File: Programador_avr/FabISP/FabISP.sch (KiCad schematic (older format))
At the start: 7 parts

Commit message: componentes completos
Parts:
- removed IC?: REGULATORSOT23, fab:fab-SOT23, symbol fab:REGULATORSOT23
- added D? (x3): DIODESOD123, fab:fab-SOD123, symbol fab:DIODESOD123
- added R?: RES-US1206FAB, fab:fab-R1206FAB, symbol fab:RES-US1206FAB
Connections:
- net labels added: GND, VCC
- wire segments 0 -> 3
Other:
- moved on the sheet: C?, JP?, M?, U?
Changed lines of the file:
@@
 L fab:ATSAMD11D14A-SS U?
 U 1 1 5F6E3135
-P 2350 1950
-F 0 "U?" H 2350 2931 50  0000 C CNN
-F 1 "ATSAMD11D14A-SS" H 2350 2840 50  0000 C CNN
-F 2 "fab:fab-SOIC-20_7.5x12.8mm_P1.27mm" H 2350 800 50  0001 C CNN
-F 3 "" H 2350 1050 50  0001 C CNN
-	1    2350 1950
+P 3100 1650
+F 0 "U?" H 3450 2400 50  0000 C CNN
+F 1 "ATSAMD11D14A-SS" H 3050 2400 50  0000 C CNN
+F 2 "fab:fab-SOIC-20_7.5x12.8mm_P1.27mm" H 3100 500 50  0001 C CNN
+F 3 "" H 3100 750 50  0001 C CNN
+	1    3100 1650
 	1    0    0    -1
 $EndComp
@@
 L fab:USB_MINIB M?
 U 1 1 5F6E4482
-P 1250 1900
-F 0 "M?" H 1250 1900 45  0001 C CNN
-F 1 "USB_MINIB" H 1250 1900 45  0001 C CNN
-F 2 "fab:fab-USB_MINIB" H 1280 2050 20  0001 C CNN
-F 3 "" H 1250 1900 50  0001 C CNN
-	1    1250 1900
-	-1   0    0    1
+P 1150 1900
+F 0 "M?" H 1379 1792 45  0001 L CNN
+F 1 "USB_MINIB" H 1150 1900 45  0001 C CNN
+F 2 "fab:fab-USB_MINIB" H 1180 2050 20  0001 C CNN
+F 3 "" H 1150 1900 50  0001 C CNN
+	1    1150 1900
+	0    -1   -1   0
 $EndComp
 $Comp
@@
 L fab:RESONATOR M?
 U 1 1 5F6E8255
-P 4700 1700
-F 0 "M?" H 4700 1954 45  0000 C CNN
-F 1 "RESONATOR" H 4700 1870 45  0000 C CNN
-F 2 "fab:fab-EFOBM" H 4730 1850 20  0001 C CNN
-F 3 "" H 4700 1700 50  0001 C CNN
-	1    4700 1700
+P 5300 1100
+F 0 "M?" H 5300 1354 45  0000 C CNN
+F 1 "RESONATOR" H 5300 1270 45  0000 C CNN
+F 2 "fab:fab-EFOBM" H 5330 1250 20  0001 C CNN
+F 3 "" H 5300 1100 50  0001 C CNN
+	1    5300 1100
 	1    0    0    -1
 $EndComp
@@
 L fab:PINHD-2X3-SMD JP?
 U 1 1 5F6E99D1
-P 4650 2600
-F 0 "JP?" H 4700 2954 45  0000 C CNN
-F 1 "PINHD-2X3-SMD" H 4700 2870 45  0000 C CNN
-F 2 "fab:fab-2X03SMD" H 4680 2750 20  0001 C CNN
-F 3 "" H 4650 2600 50  0001 C CNN
-	1    4650 2600
-	1    0    0    -1
-$EndComp
-$Comp
-L fab:REGULATORSOT23 IC?
-U 1 1 5F6EA6B2
-P 5750 2000
-F 0 "IC?" H 5750 2354 45  0000 C CNN
-F 1 "REGULATORSOT23" H 5750 2270 45  0000 C CNN
-F 2 "fab:fab-SOT23" H 5780 2150 20  0001 C CNN
-F 3 "" H 5750 2000 50  0001 C CNN
-	1    5750 2000
+P 2100 2400
+F 0 "JP?" H 2150 2754 45  0000 C CNN
+F 1 "PINHD-2X3-SMD" H 2150 2670 45  0000 C CNN
+F 2 "fab:fab-2X03SMD" H 2130 2550 20  0001 C CNN
+F 3 "" H 2100 2400 50  0001 C CNN
+	1    2100 2400
 	1    0    0    -1
 $EndComp
@@
 L fab:CAP-US1206FAB C?
 U 1 1 5F6EB467
-P 3600 2800
-F 0 "C?" H 3650 3054 45  0000 C CNN
-F 1 "CAP-US1206FAB" H 3650 2970 45  0000 C CNN
-F 2 "fab:fab-C1206FAB" H 3630 2950 20  0001 C CNN
-F 3 "" H 3600 2800 50  0001 C CNN
-	1    3600 2800
+P 1750 1300
+F 0 "C?" V 1758 1428 45  0000 L CNN
+F 1 "CAP-US1206FAB" V 1842 1428 45  0000 L CNN
+F 2 "fab:fab-C1206FAB" H 1780 1450 20  0001 C CNN
+F 3 "" H 1750 1300 50  0001 C CNN
+	1    1750 1300
+	0    1    1    0
+$EndComp
+$Comp
+L fab:DIODESOD123 D?
+U 1 1 5F6EC2CB
+P 5150 2200
+F 0 "D?" V 5192 2122 45  0000 R CNN
+F 1 "DIODESOD123" V 5108 2122 45  0000 R CNN
+F 2 "fab:fab-SOD123" H 5180 2350 20  0001 C CNN
+F 3 "" H 5150 2200 50  0001 C CNN
+	1    5150 2200
+	0    -1   -1   0
+$EndComp
+$Comp
+L power:VCC #PWR?
+U 1 1 5F6EDF62
+P 1500 1100
+F 0 "#PWR?" H 1500 950 50  0001 C CNN
+F 1 "VCC" H 1517 1273 50  0000 C CNN
+F 2 "" H 1500 1100 50  0001 C CNN
+F 3 "" H 1500 1100 50  0001 C CNN
+	1    1500 1100
 	1    0    0    -1
 $EndComp
+$Comp
+L power:GND #PWR?
+U 1 1 5F6EEE4A
+P 3100 2450
+F 0 "#PWR?" H 3100 2200 50  0001 C CNN
+F 1 "GND" H 3105 2277 50  0000 C CNN
+F 2 "" H 3100 2450 50  0001 C CNN
+F 3 "" H 3100 2450 50  0001 C CNN
+	1    3100 2450
+	1    0    0    -1
+$EndComp
+$Comp
+L power:VCC #PWR?
+U 1 1 5F6F2122
+P 3100 850
+F 0 "#PWR?" H 3100 700 50  0001 C CNN
+F 1 "VCC" H 3117 1023 50  0000 C CNN
+F 2 "" H 3100 850 50  0001 C CNN
+F 3 "" H 3100 850 50  0001 C CNN
+	1    3100 850
+	1    0    0    -1
+$EndComp
+$Comp
+L fab:RES-US1206FAB R?
+U 1 1 5F6FE07F
+P 1350 2250
+F 0 "R?" V 1308 2318 45  0000 L CNN
+F 1 "RES-US1206FAB" H 950 2200 45  0000 L CNN
+F 2 "fab:fab-R1206FAB" H 1380 2400 20  0001 C CNN
+F 3 "" H 1350 2250 50  0001 C CNN
+	1    1350 2250
+	-1   0    0    1
+$EndComp
+$Comp
+L fab:DIODESOD123 D?
+U 1 1 5F700804
+P 1150 2450
+F 0 "D?" V 1108 2528 45  0000 L CNN
+F 1 "DIODESOD123" V 1192 2528 45  0000 L CNN
+F 2 "fab:fab-SOD123" H 1180 2600 20  0001 C CNN
+F 3 "" H 1150 2450 50  0001 C CNN
+	1    1150 2450
+	0    1    1    0
+$EndComp
+Wire Wire Line
+	1150 2000 1150 2250
+Wire Wire Line
+	1150 2350 1150 2250
+Connection ~ 1150 2250
+$Comp
+L power:GND #PWR?
+U 1 1 5F7029DD
+P 1150 2700
+F 0 "#PWR?" H 1150 2450 50  0001 C CNN
+F 1 "GND" H 1155 2527 50  0000 C CNN
+F 2 "" H 1150 2700 50  0001 C CNN
+F 3 "" H 1150 2700 50  0001 C CNN
+	1    1150 2700
+	1    0    0    -1
+$EndComp
+Wire Wire Line
+	1150 2550 1150 2700
+$Comp
+L fab:DIODESOD123 D?
+U 1 1 5F70324B
+P 950 2450
+F 0 "D?" V 908 2528 45  0000 L CNN
+F 1 "DIODESOD123" V 992 2528 45  0000 L CNN
+F 2 "fab:fab-SOD123" H 980 2600 20  0001 C CNN
+F 3 "" H 950 2450 50  0001 C CNN
+	1    950  2450
+	0    1    1    0
+$EndComp
 $EndSCHEMATC

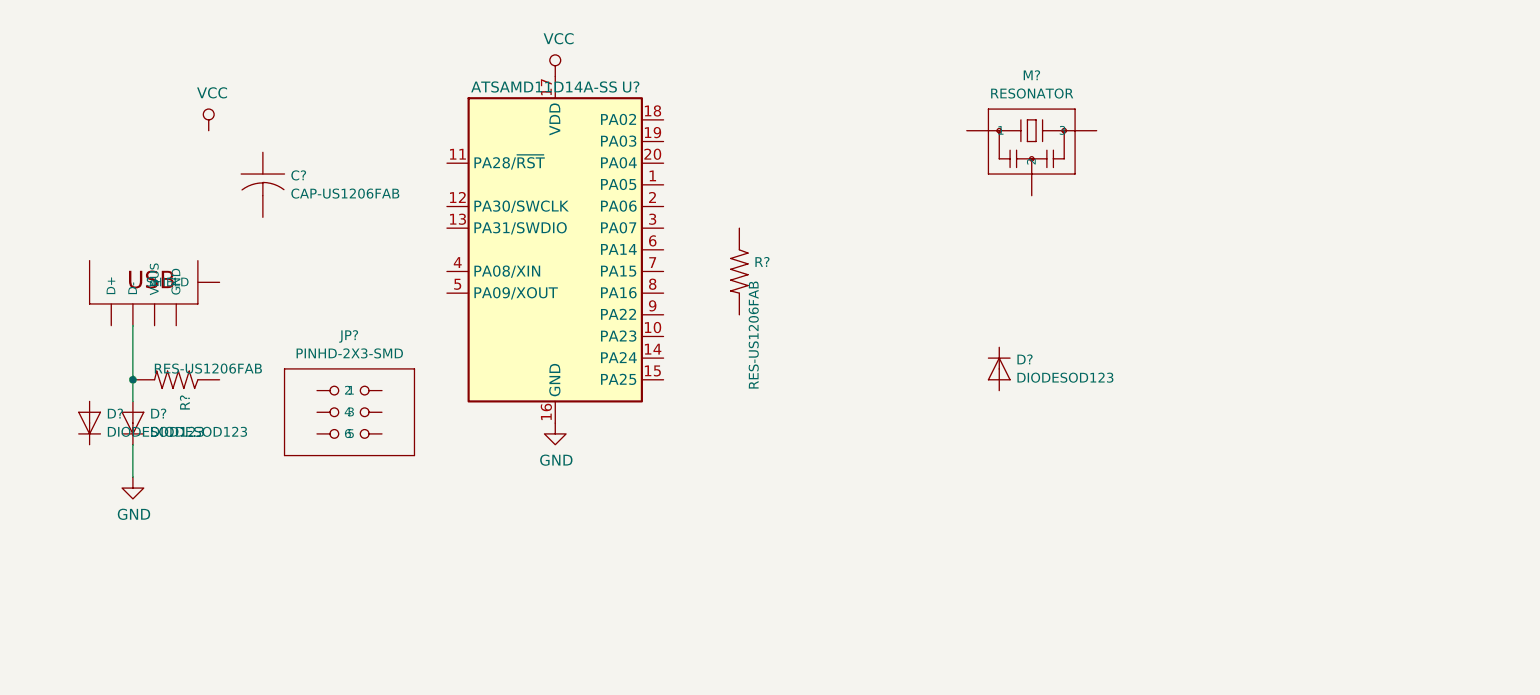
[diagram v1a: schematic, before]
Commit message: Conexiones USB
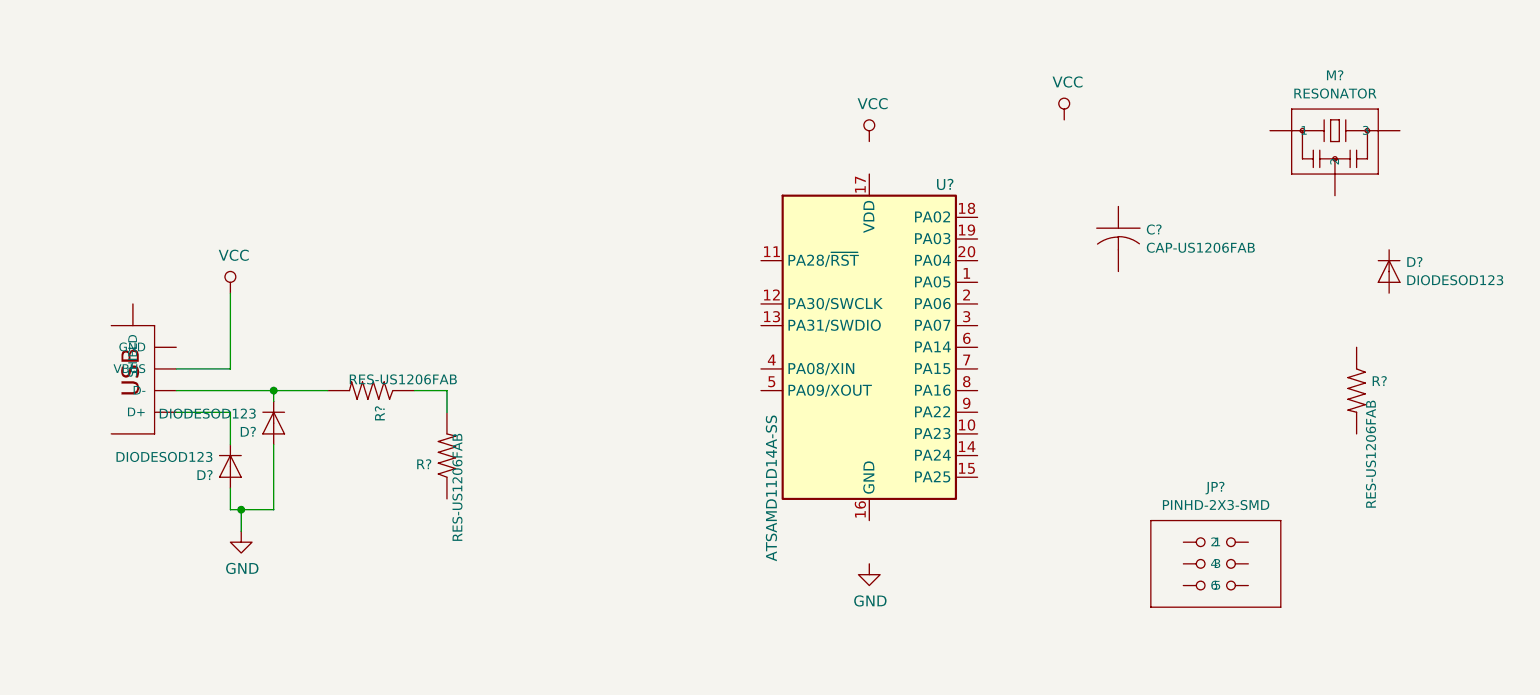
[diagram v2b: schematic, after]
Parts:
- added R?: RES-US1206FAB, fab:fab-R1206FAB, symbol fab:RES-US1206FAB
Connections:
- net GND: now also D?.ANODE (A), D?.ANODE (A); no longer D?.CATHODE (C), U?.16 (GND)
- net VCC: now also M?.VBUS; no longer U?.17 (VDD)
- net at M?.D+: now also D?.CATHODE (C)
- net at M?.D-, R?.2: now also D?.CATHODE (C); no longer D?.ANODE (A)
- net at R?.1: now also R?.2
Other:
- moved on the sheet: C?, D?, JP?, M?, R?, U?
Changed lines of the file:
@@
 EESchema Schematic File Version 4
+LIBS:FabISP-cache
 EELAYER 30 0
 EELAYER END
@@
 L fab:ATSAMD11D14A-SS U?
 U 1 1 5F6E3135
-P 3100 1650
-F 0 "U?" H 3450 2400 50  0000 C CNN
-F 1 "ATSAMD11D14A-SS" H 3050 2400 50  0000 C CNN
-F 2 "fab:fab-SOIC-20_7.5x12.8mm_P1.27mm" H 3100 500 50  0001 C CNN
-F 3 "" H 3100 750 50  0001 C CNN
-	1    3100 1650
+P 4550 2100
+F 0 "U?" H 4900 2850 50  0000 C CNN
+F 1 "ATSAMD11D14A-SS" V 4100 1450 50  0000 C CNN
+F 2 "fab:fab-SOIC-20_7.5x12.8mm_P1.27mm" H 4550 950 50  0001 C CNN
+F 3 "" H 4550 1200 50  0001 C CNN
+	1    4550 2100
 	1    0    0    -1
 $EndComp
@@
 L fab:USB_MINIB M?
 U 1 1 5F6E4482
-P 1150 1900
-F 0 "M?" H 1379 1792 45  0001 L CNN
-F 1 "USB_MINIB" H 1150 1900 45  0001 C CNN
-F 2 "fab:fab-USB_MINIB" H 1180 2050 20  0001 C CNN
-F 3 "" H 1150 1900 50  0001 C CNN
-	1    1150 1900
-	0    -1   -1   0
+P 1250 2300
+F 0 "M?" H 1479 2192 45  0001 L CNN
+F 1 "USB_MINIB" H 1250 2300 45  0001 C CNN
+F 2 "fab:fab-USB_MINIB" H 1280 2450 20  0001 C CNN
+F 3 "" H 1250 2300 50  0001 C CNN
+	1    1250 2300
+	-1   0    0    1
 $EndComp
 $Comp
 L fab:RES-US1206FAB R?
 U 1 1 5F6E5992
-P 3950 1750
-F 0 "R?" V 3908 1818 45  0000 L CNN
-F 1 "RES-US1206FAB" H 3992 1818 45  0000 L CNN
-F 2 "fab:fab-R1206FAB" H 3980 1900 20  0001 C CNN
-F 3 "" H 3950 1750 50  0001 C CNN
-	1    3950 1750
+P 6800 2300
+F 0 "R?" V 6758 2368 45  0000 L CNN
+F 1 "RES-US1206FAB" H 6842 2368 45  0000 L CNN
+F 2 "fab:fab-R1206FAB" H 6830 2450 20  0001 C CNN
+F 3 "" H 6800 2300 50  0001 C CNN
+	1    6800 2300
 	0    1    1    0
 $EndComp
@@
 L fab:RESONATOR M?
 U 1 1 5F6E8255
-P 5300 1100
-F 0 "M?" H 5300 1354 45  0000 C CNN
-F 1 "RESONATOR" H 5300 1270 45  0000 C CNN
-F 2 "fab:fab-EFOBM" H 5330 1250 20  0001 C CNN
-F 3 "" H 5300 1100 50  0001 C CNN
-	1    5300 1100
+P 6700 1100
+F 0 "M?" H 6700 1354 45  0000 C CNN
+F 1 "RESONATOR" H 6700 1270 45  0000 C CNN
+F 2 "fab:fab-EFOBM" H 6730 1250 20  0001 C CNN
+F 3 "" H 6700 1100 50  0001 C CNN
+	1    6700 1100
 	1    0    0    -1
 $EndComp
@@
 L fab:PINHD-2X3-SMD JP?
 U 1 1 5F6E99D1
-P 2100 2400
-F 0 "JP?" H 2150 2754 45  0000 C CNN
-F 1 "PINHD-2X3-SMD" H 2150 2670 45  0000 C CNN
-F 2 "fab:fab-2X03SMD" H 2130 2550 20  0001 C CNN
-F 3 "" H 2100 2400 50  0001 C CNN
-	1    2100 2400
+P 6100 3100
+F 0 "JP?" H 6150 3454 45  0000 C CNN
+F 1 "PINHD-2X3-SMD" H 6150 3370 45  0000 C CNN
+F 2 "fab:fab-2X03SMD" H 6130 3250 20  0001 C CNN
+F 3 "" H 6100 3100 50  0001 C CNN
+	1    6100 3100
 	1    0    0    -1
 $EndComp
@@
 L fab:CAP-US1206FAB C?
 U 1 1 5F6EB467
-P 1750 1300
-F 0 "C?" V 1758 1428 45  0000 L CNN
-F 1 "CAP-US1206FAB" V 1842 1428 45  0000 L CNN
-F 2 "fab:fab-C1206FAB" H 1780 1450 20  0001 C CNN
-F 3 "" H 1750 1300 50  0001 C CNN
-	1    1750 1300
+P 5700 1550
+F 0 "C?" V 5708 1678 45  0000 L CNN
+F 1 "CAP-US1206FAB" V 5792 1678 45  0000 L CNN
+F 2 "fab:fab-C1206FAB" H 5730 1700 20  0001 C CNN
+F 3 "" H 5700 1550 50  0001 C CNN
+	1    5700 1550
 	0    1    1    0
 $EndComp
@@
 L fab:DIODESOD123 D?
 U 1 1 5F6EC2CB
-P 5150 2200
-F 0 "D?" V 5192 2122 45  0000 R CNN
-F 1 "DIODESOD123" V 5108 2122 45  0000 R CNN
-F 2 "fab:fab-SOD123" H 5180 2350 20  0001 C CNN
-F 3 "" H 5150 2200 50  0001 C CNN
-	1    5150 2200
+P 6950 1750
+F 0 "D?" V 6992 1672 45  0000 R CNN
+F 1 "DIODESOD123" V 6908 1672 45  0000 R CNN
+F 2 "fab:fab-SOD123" H 6980 1900 20  0001 C CNN
+F 3 "" H 6950 1750 50  0001 C CNN
+	1    6950 1750
 	0    -1   -1   0
 $EndComp
@@
 L power:VCC #PWR?
 U 1 1 5F6EDF62
-P 1500 1100
-F 0 "#PWR?" H 1500 950 50  0001 C CNN
-F 1 "VCC" H 1517 1273 50  0000 C CNN
-F 2 "" H 1500 1100 50  0001 C CNN
-F 3 "" H 1500 1100 50  0001 C CNN
-	1    1500 1100
+P 5450 1050
+F 0 "#PWR?" H 5450 900 50  0001 C CNN
+F 1 "VCC" H 5467 1223 50  0000 C CNN
+F 2 "" H 5450 1050 50  0001 C CNN
+F 3 "" H 5450 1050 50  0001 C CNN
+	1    5450 1050
 	1    0    0    -1
 $EndComp
@@
 L power:GND #PWR?
 U 1 1 5F6EEE4A
-P 3100 2450
-F 0 "#PWR?" H 3100 2200 50  0001 C CNN
-F 1 "GND" H 3105 2277 50  0000 C CNN
-F 2 "" H 3100 2450 50  0001 C CNN
-F 3 "" H 3100 2450 50  0001 C CNN
-	1    3100 2450
+P 4550 3100
+F 0 "#PWR?" H 4550 2850 50  0001 C CNN
+F 1 "GND" H 4555 2927 50  0000 C CNN
+F 2 "" H 4550 3100 50  0001 C CNN
+F 3 "" H 4550 3100 50  0001 C CNN
+	1    4550 3100
 	1    0    0    -1
 $EndComp
@@
 L power:VCC #PWR?
 U 1 1 5F6F2122
-P 3100 850
-F 0 "#PWR?" H 3100 700 50  0001 C CNN
-F 1 "VCC" H 3117 1023 50  0000 C CNN
-F 2 "" H 3100 850 50  0001 C CNN
-F 3 "" H 3100 850 50  0001 C CNN
-	1    3100 850
+P 4550 1150
+F 0 "#PWR?" H 4550 1000 50  0001 C CNN
+F 1 "VCC" H 4567 1323 50  0000 C CNN
+F 2 "" H 4550 1150 50  0001 C CNN
+F 3 "" H 4550 1150 50  0001 C CNN
+	1    4550 1150
 	1    0    0    -1
 $EndComp
@@
 L fab:RES-US1206FAB R?
 U 1 1 5F6FE07F
-P 1350 2250
-F 0 "R?" V 1308 2318 45  0000 L CNN
-F 1 "RES-US1206FAB" H 950 2200 45  0000 L CNN
-F 2 "fab:fab-R1206FAB" H 1380 2400 20  0001 C CNN
-F 3 "" H 1350 2250 50  0001 C CNN
-	1    1350 2250
+P 2250 2300
+F 0 "R?" V 2208 2368 45  0000 L CNN
+F 1 "RES-US1206FAB" H 1850 2250 45  0000 L CNN
+F 2 "fab:fab-R1206FAB" H 2280 2450 20  0001 C CNN
+F 3 "" H 2250 2300 50  0001 C CNN
+	1    2250 2300
 	-1   0    0    1
 $EndComp
@@
 L fab:DIODESOD123 D?
 U 1 1 5F700804
-P 1150 2450
-F 0 "D?" V 1108 2528 45  0000 L CNN
-F 1 "DIODESOD123" V 1192 2528 45  0000 L CNN
-F 2 "fab:fab-SOD123" H 1180 2600 20  0001 C CNN
-F 3 "" H 1150 2450 50  0001 C CNN
-	1    1150 2450
-	0    1    1    0
-$EndComp
-Wire Wire Line
-	1150 2000 1150 2250
-Wire Wire Line
-	1150 2350 1150 2250
-Connection ~ 1150 2250
+P 1800 2450
+F 0 "D?" V 1758 2528 45  0000 L CNN
+F 1 "DIODESOD123" V 1842 2528 45  0000 L CNN
+F 2 "fab:fab-SOD123" H 1830 2600 20  0001 C CNN
+F 3 "" H 1800 2450 50  0001 C CNN
+	1    1800 2450
+	0    -1   -1   0
+$EndComp
 $Comp
 L power:GND #PWR?
 U 1 1 5F7029DD
-P 1150 2700
-F 0 "#PWR?" H 1150 2450 50  0001 C CNN
-F 1 "GND" H 1155 2527 50  0000 C CNN
-F 2 "" H 1150 2700 50  0001 C CNN
-F 3 "" H 1150 2700 50  0001 C CNN
-	1    1150 2700
-	1    0    0    -1
-$EndComp
-Wire Wire Line
-	1150 2550 1150 2700
+P 1650 2950
+F 0 "#PWR?" H 1650 2700 50  0001 C CNN
+F 1 "GND" H 1655 2777 50  0000 C CNN
+F 2 "" H 1650 2950 50  0001 C CNN
+F 3 "" H 1650 2950 50  0001 C CNN
+	1    1650 2950
+	1    0    0    -1
+$EndComp
 $Comp
 L fab:DIODESOD123 D?
 U 1 1 5F70324B
-P 950 2450
-F 0 "D?" V 908 2528 45  0000 L CNN
-F 1 "DIODESOD123" V 992 2528 45  0000 L CNN
-F 2 "fab:fab-SOD123" H 980 2600 20  0001 C CNN
-F 3 "" H 950 2450 50  0001 C CNN
-	1    950  2450
-	0    1    1    0
-$EndComp
+P 1600 2650
+F 0 "D?" V 1558 2728 45  0000 L CNN
+F 1 "DIODESOD123" V 1642 2728 45  0000 L CNN
+F 2 "fab:fab-SOD123" H 1630 2800 20  0001 C CNN
+F 3 "" H 1600 2650 50  0001 C CNN
+	1    1600 2650
+	0    -1   -1   0
+$EndComp
+$Comp
+L power:VCC #PWR?
+U 1 1 5F8A1864
+P 1600 1850
+F 0 "#PWR?" H 1600 1700 50  0001 C CNN
+F 1 "VCC" H 1617 2023 50  0000 C CNN
+F 2 "" H 1600 1850 50  0001 C CNN
+F 3 "" H 1600 1850 50  0001 C CNN
+	1    1600 1850
+	1    0    0    -1
+$EndComp
+Wire Wire Line
+	1350 2400 1600 2400
+Wire Wire Line
+	1600 2400 1600 2550
+Wire Wire Line
+	1350 2300 1800 2300
+Wire Wire Line
+	1800 2350 1800 2300
+Connection ~ 1800 2300
+Wire Wire Line
+	1800 2300 2050 2300
+Wire Wire Line
+	1650 2850 1600 2850
+Wire Wire Line
+	1600 2850 1600 2750
+Wire Wire Line
+	1650 2850 1800 2850
+Wire Wire Line
+	1800 2850 1800 2550
+Connection ~ 1650 2850
+Wire Wire Line
+	1650 2850 1650 2950
+$Comp
+L fab:RES-US1206FAB R?
+U 1 1 5F8A9CBD
+P 2600 2600
+F 0 "R?" V 2558 2668 45  0000 L CNN
+F 1 "RES-US1206FAB" H 2200 2550 45  0000 L CNN
+F 2 "fab:fab-R1206FAB" H 2630 2750 20  0001 C CNN
+F 3 "" H 2600 2600 50  0001 C CNN
+	1    2600 2600
+	0    -1   -1   0
+$EndComp
+Wire Wire Line
+	2450 2300 2600 2300
+Wire Wire Line
+	2600 2300 2600 2400
+Wire Wire Line
+	1350 2200 1600 2200
+Wire Wire Line
+	1600 2200 1600 1850
 $EndSCHEMATC

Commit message: Conexiones completas queda Pendiente agregar etiquetas
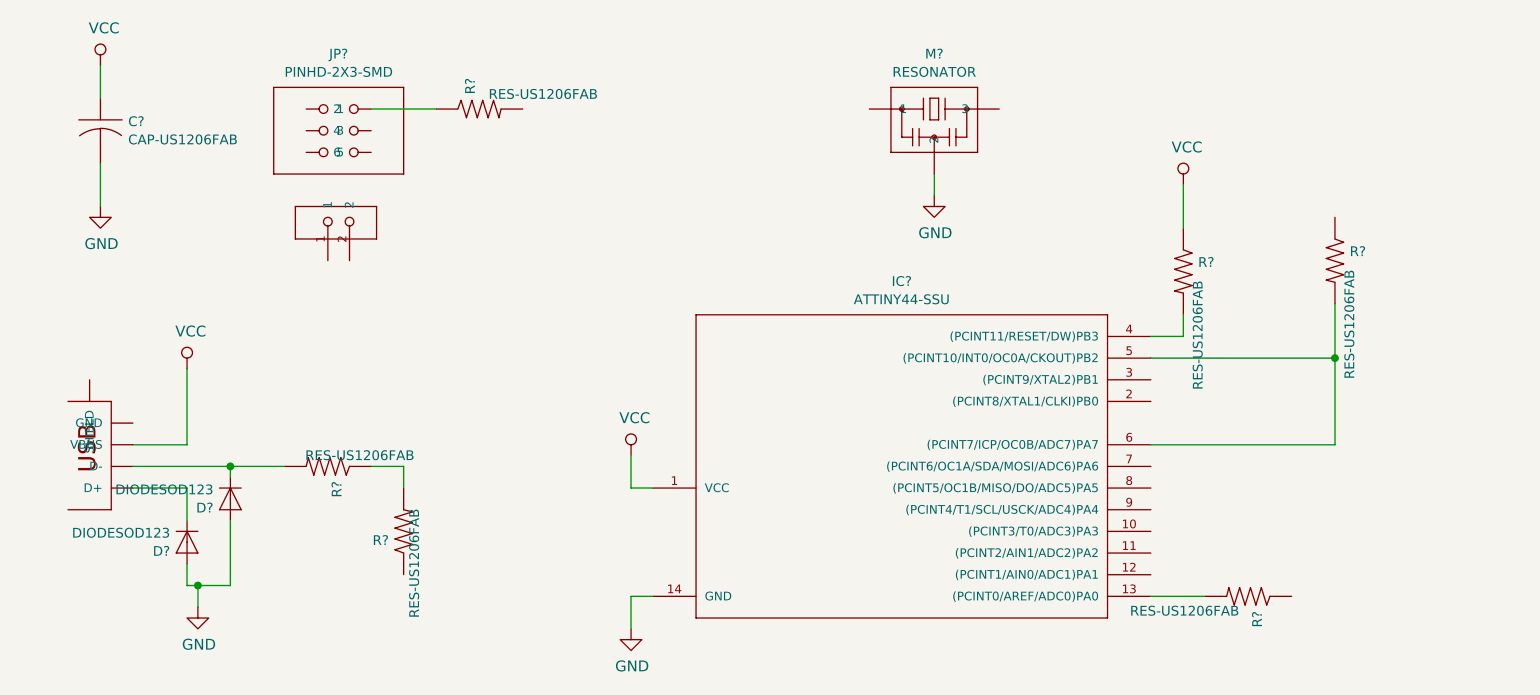
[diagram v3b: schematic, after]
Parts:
- removed D?: DIODESOD123, fab:fab-SOD123, symbol fab:DIODESOD123
- removed U?: ATSAMD11D14A-SS, fab:fab-SOIC-20_7.5x12.8mm_P1.27mm, symbol fab:ATSAMD11D14A-SS
- added IC?: ATTINY44-SSU, fab:fab-SOIC-14_3.9x8.7mm_P1.27mm, symbol fab:ATTINY44-SSU
- added M?: PINHD-1x02-SMD-HEADER, fab:fab-1X02SMD, symbol fab:PINHD-1x02-SMD-HEADER
- added R? (x3): RES-US1206FAB, fab:fab-R1206FAB, symbol fab:RES-US1206FAB
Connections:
- net GND: now also C?.2, M?.2, IC?.14 (GND)
- net VCC: now also C?.1, IC?.1 (VCC), R?.1
- net at R?.1: now also JP?.2
- new net: IC?.5 ((PCINT10/INT0/OC0A/CKOUT)PB2), IC?.6 ((PCINT7/ICP/OC0B/ADC7)PA7), R?.2
- new net: IC?.13 ((PCINT0/AREF/ADC0)PA0), R?.2
- new net: IC?.4 ((PCINT11/RESET/DW)PB3), R?.2
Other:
- moved on the sheet: C?, D?, JP?, M?, R?
